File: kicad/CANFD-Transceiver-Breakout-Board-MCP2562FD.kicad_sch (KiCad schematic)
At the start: 18 parts, among them J2 1862042, K1 HEADER_MALE_6X1, U1 MCP2562FD-E_SN

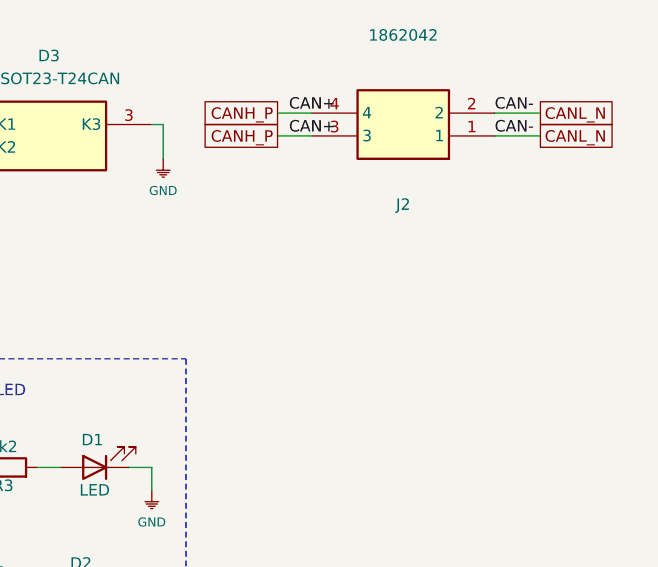
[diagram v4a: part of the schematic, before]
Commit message: v2 with jst connector
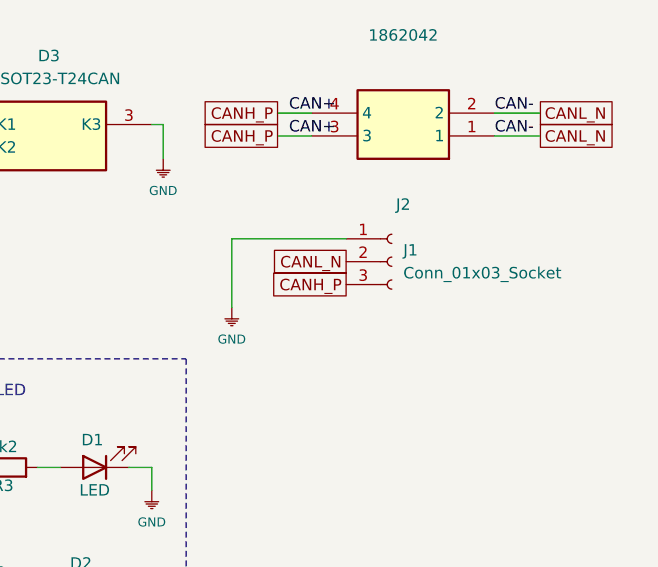
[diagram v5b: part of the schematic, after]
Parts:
- added J1: Conn_01x03_Socket, Connector_JST:JST_PH_S3B-PH-K_1x03_P2.00mm_Horizontal, symbol Connector:Conn_01x03_Socket
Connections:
- net CANH_P: now also J1.3 (Pin_3)
- net CANL_N: now also J1.2 (Pin_2)
- net GND: now also J1.1 (Pin_1)
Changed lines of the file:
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@@
 	(wire
 		(pts
+			(xy 251.46 85.09) (xy 238.76 85.09)
+		)
+		(stroke
+			(width 0)
+			(type default)
+		)
+	)
+	(wire
+		(pts
 			(xy 137.16 57.15) (xy 139.7 57.15)
 		)
@@
 	(wire
 		(pts
+			(xy 238.76 85.09) (xy 238.76 92.71)
+		)
+		(stroke
+			(width 0)
+			(type default)
+		)
+	)
+	(wire
+		(pts
 			(xy 96.52 64.77) (xy 106.68 64.77)
 		)
@@
 		)
 	)
+	(global_label "CANH_P"
+		(shape passive)
+		(at 251.46 90.17 180)
+		(effects
+			(font
+				(size 1.27 1.27)
+			)
+			(justify right)
+		)
+		(property "Intersheetrefs" "${INTERSHEET_REFS}"
+			(at 242.5034 90.2494 0)
+			(effects
+				(font
+					(size 1.27 1.27)
+				)
+				(justify right)
+				(hide yes)
+			)
+		)
+	)
 	(global_label "5V"
 		(shape input)
@@
 	(global_label "CANL_N"
 		(shape passive)
+		(at 251.46 87.63 180)
+		(effects
+			(font
+				(size 1.27 1.27)
+			)
+			(justify right)
+		)
+		(property "Intersheetrefs" "${INTERSHEET_REFS}"
+			(at 242.8058 87.7094 0)
+			(effects
+				(font
+					(size 1.27 1.27)
+				)
+				(justify right)
+				(hide yes)
+			)
+		)
+	)
+	(global_label "CANL_N"
+		(shape passive)
 		(at 184.15 85.09 270)
 		(effects
@@
 	)
 	(symbol
+		(lib_name "e-radionica.com schematics:GND_3")
+		(lib_id "e-radionica.com schematics:GND")
+		(at 238.76 92.71 0)
+		(unit 1)
+		(exclude_from_sim no)
+		(in_bom yes)
+		(on_board yes)
+		(dnp no)
+		(property "Reference" "#PWR015"
+			(at 243.205 92.71 0)
+			(effects
+				(font
+					(size 1 1)
+				)
+				(hide yes)
+			)
+		)
+		(property "Value" "GND"
+			(at 238.76 96.266 0)
+			(effects
+				(font
+					(size 1 1)
+				)
+			)
+		)
+		(property "Footprint" ""
+			(at 243.205 88.9 0)
+			(effects
+				(font
+					(size 1 1)
+				)
+				(hide yes)
+			)
+		)
+		(property "Datasheet" ""
+			(at 243.205 88.9 0)
+			(effects
+				(font
+					(size 1 1)
+				)
+				(hide yes)
+			)
+		)
+		(property "Description" ""
+			(at 238.76 92.71 0)
+			(effects
+				(font
+					(size 1.27 1.27)
+				)
+			)
+		)
+		(pin "1"
+		)
+		(instances
+			(project "CANFD-Transceiver-Breakout-Board-MCP2562FD"
+				(path "/802bf3dd-45f4-457b-8e6e-ea2d44622c13"
+					(reference "#PWR015")
+					(unit 1)
+				)
+			)
+		)
+	)
+	(symbol
 		(lib_id "e-radionica.com schematics:GND")
 		(at 132.08 77.47 0)
@@
 					(unit 1)
 				)
+			)
+		)
+	)
+	(symbol
+		(lib_id "Connector:Conn_01x03_Socket")
+		(at 256.54 87.63 0)
+		(unit 1)
+		(exclude_from_sim no)
+		(in_bom yes)
+		(on_board yes)
+		(dnp no)
+		(fields_autoplaced yes)
+		(property "Reference" "J1"
+			(at 257.81 86.3599 0)
+			(effects
+				(font
+					(size 1.27 1.27)
+				)
+				(justify left)
+			)
+		)
+		(property "Value" "Conn_01x03_Socket"
+			(at 257.81 88.8999 0)
+			(effects
+				(font
+					(size 1.27 1.27)
+				)
+				(justify left)
+			)
+		)
+		(property "Footprint" "Connector_JST:JST_PH_S3B-PH-K_1x03_P2.00mm_Horizontal"
+			(at 256.54 87.63 0)
+			(effects
+				(font
+					(size 1.27 1.27)
+				)
+				(hide yes)
+			)
+		)
+		(property "Datasheet" "~"
+			(at 256.54 87.63 0)
+			(effects
+				(font
+					(size 1.27 1.27)
+				)
+				(hide yes)
+			)
+		)
+		(property "Description" "Generic connector, single row, 01x03, script generated"
+			(at 256.54 87.63 0)
+			(effects
+				(font
+					(size 1.27 1.27)
+				)
+				(hide yes)
+			)
+		)
+		(pin "3"
+		)
+		(pin "2"
+		)
+		(pin "1"
+		)
+		(instances
+			(project "CANFD-Transceiver-Breakout-Board-MCP2562FD"
+				(path "/802bf3dd-45f4-457b-8e6e-ea2d44622c13"
+					(reference "J1")
+					(unit 1)
+				)
